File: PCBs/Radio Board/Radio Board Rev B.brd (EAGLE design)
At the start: 95.9 x 90.2 mm, 4 parts

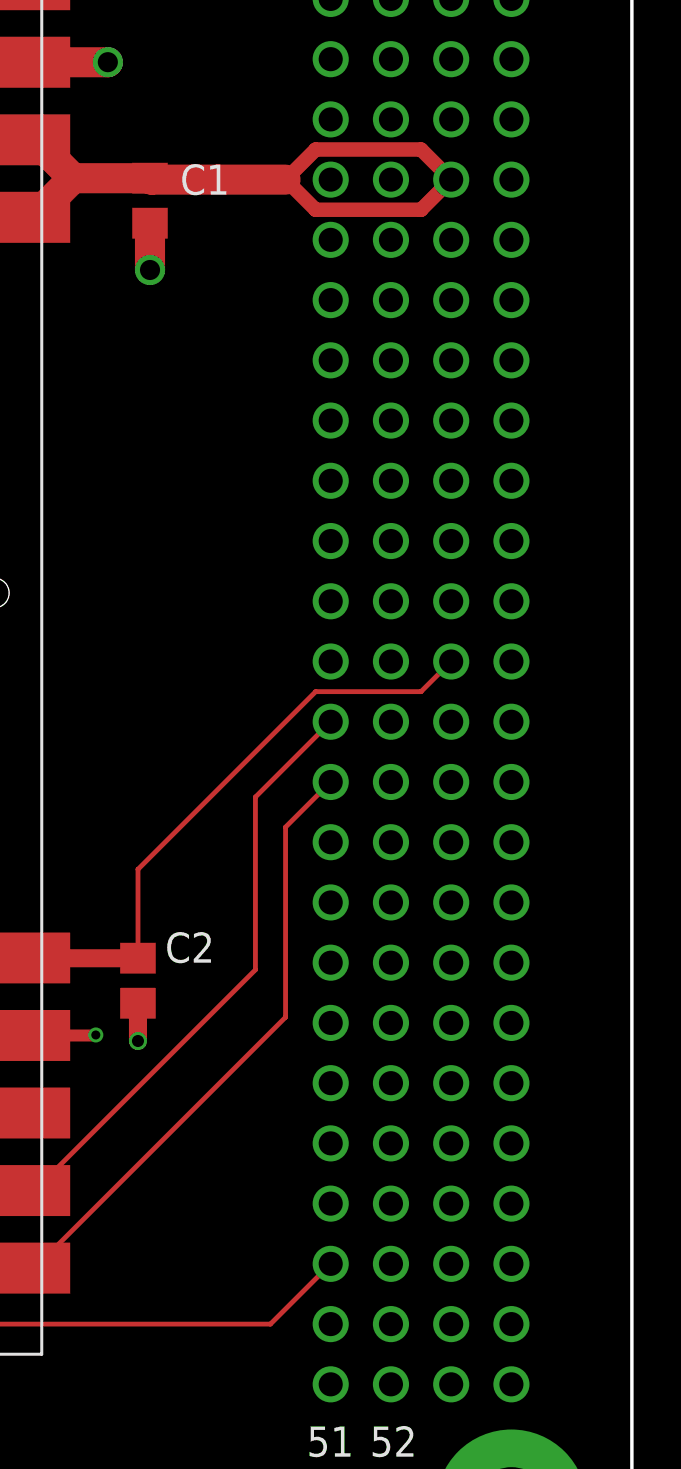
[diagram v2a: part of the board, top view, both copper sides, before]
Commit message: Use common PC104 footprint with dimensions set per board
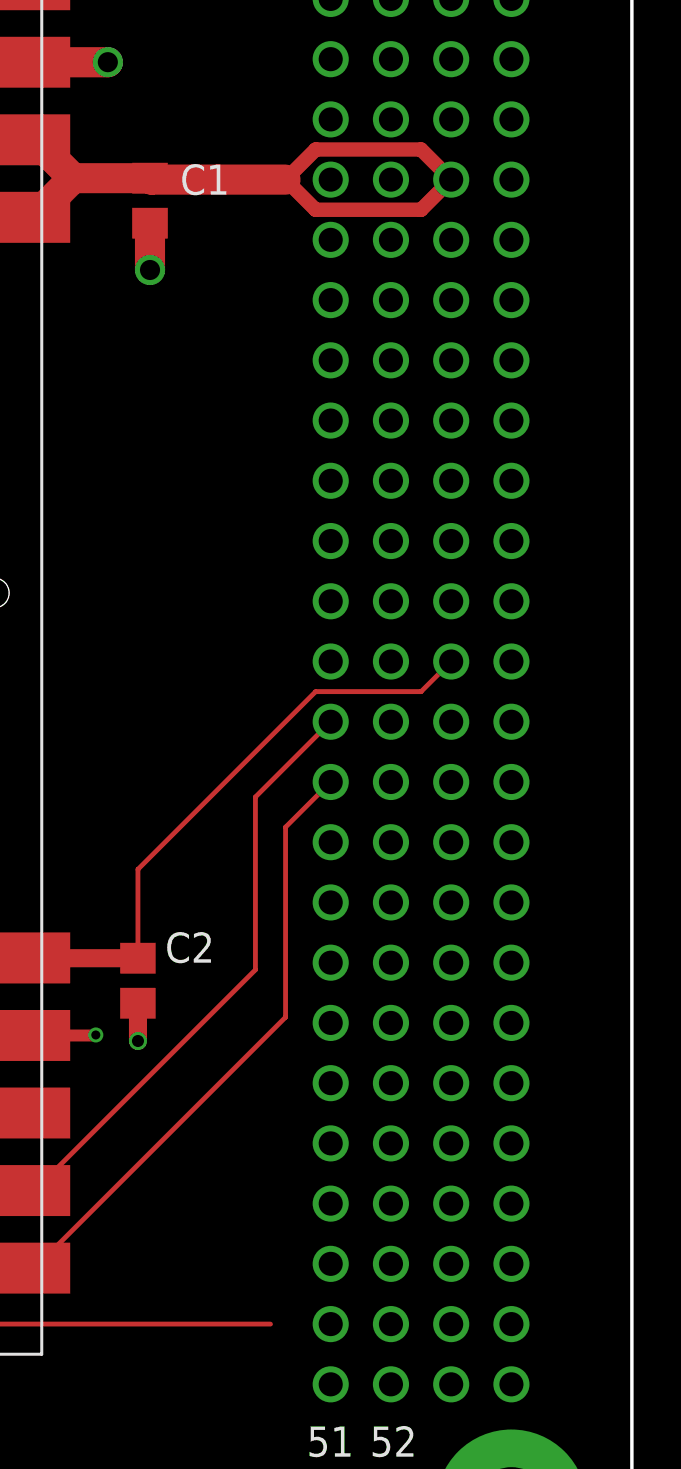
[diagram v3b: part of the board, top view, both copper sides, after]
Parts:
- removed U$2: PC104_RADIO, Cubesat:PC104_RADIO
- added U$1: PC104_NO_DIMENSION, Cubesat:PC104_NO_DIMENSION
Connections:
- net 3V3: now also U$1.79; no longer U$2.79
- net GND: now also U$1.100, U$1.61, U$1.66, U$1.69, U$1.73, U$1.74, U$1.81, U$1.82, U$1.84, U$1.99; no longer U$2.100, U$2.61, U$2.66, U$2.69, U$2.73, U$2.74, U$2.81, U$2.82, U$2.84, U$2.99
- net LITHIUM_RX: now also U$1.29; no longer U$2.29
- net LITHIUM_TX: now also U$1.31; no longer U$2.31
- net OA_RESET: now also U$1.47; no longer U$2.47
- net SW3: now also U$1.63; no longer U$2.63
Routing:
- net OA_RESET: track 46.8 -> 43.2 mm
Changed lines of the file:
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@@
 <board>
 <plain>
+<wire x1="0" y1="85.09" x2="0" y2="5.08" width="0.127" layer="20"/>
+<wire x1="0" y1="5.08" x2="5.08" y2="0" width="0.127" layer="20" curve="90"/>
+<wire x1="5.08" y1="0" x2="90.805" y2="0" width="0.127" layer="20"/>
+<wire x1="90.805" y1="0" x2="95.885" y2="5.08" width="0.127" layer="20" curve="90"/>
+<wire x1="95.885" y1="5.08" x2="95.885" y2="85.09" width="0.127" layer="20"/>
+<wire x1="95.885" y1="85.09" x2="90.678" y2="90.17" width="0.127" layer="20" curve="91.414625"/>
+<wire x1="0" y1="85.09" x2="10.16" y2="85.09" width="0.127" layer="20" curve="-180"/>
+<wire x1="10.16" y1="85.09" x2="15.24" y2="80.01" width="0.127" layer="20" curve="90"/>
+<wire x1="15.24" y1="80.01" x2="31.75" y2="80.01" width="0.127" layer="20"/>
+<wire x1="31.75" y1="80.01" x2="36.83" y2="85.09" width="0.127" layer="20" curve="90"/>
+<wire x1="36.83" y1="85.09" x2="41.91" y2="90.17" width="0.127" layer="20" curve="-90"/>
+<wire x1="41.91" y1="90.17" x2="90.678" y2="90.17" width="0.127" layer="20"/>
 </plain>
 <attributes>
@@
 </element>
 <element name="LI-1" library="Cubesat" package="LI-1" value="LI-1" x="38.1" y="13.97"/>
-<element name="U$2" library="Cubesat" package="PC104_RADIO" value="PC104_RADIO" x="0" y="0"/>
+<element name="U$1" library="Cubesat" package="PC104_NO_DIMENSION" value="PC104_NO_DIMENSION" x="0" y="0"/>
 </elements>
 <signals>
@@
 <wire x1="73.752" y1="71.72" x2="73.787" y2="71.755" width="1.27" layer="1"/>
 <via x="73.787" y="71.755" extent="1-16" drill="0.846665625"/>
-<contactref element="U$2" pad="61"/>
-<contactref element="U$2" pad="74"/>
-<contactref element="U$2" pad="73"/>
-<contactref element="U$2" pad="66"/>
-<contactref element="U$2" pad="69"/>
-<contactref element="U$2" pad="81"/>
-<contactref element="U$2" pad="99"/>
-<contactref element="U$2" pad="82"/>
-<contactref element="U$2" pad="84"/>
-<contactref element="U$2" pad="100"/>
 <contactref element="LI-1" pad="THERM1"/>
 <contactref element="LI-1" pad="THERM2"/>
 <contactref element="LI-1" pad="THERM3"/>
 <contactref element="LI-1" pad="THERM4"/>
+<contactref element="U$1" pad="61"/>
+<contactref element="U$1" pad="74"/>
+<contactref element="U$1" pad="73"/>
+<contactref element="U$1" pad="66"/>
+<contactref element="U$1" pad="69"/>
+<contactref element="U$1" pad="81"/>
+<contactref element="U$1" pad="99"/>
+<contactref element="U$1" pad="82"/>
+<contactref element="U$1" pad="84"/>
+<contactref element="U$1" pad="100"/>
 <wire x1="45.72" y1="52.07" x2="54.4" y2="60.07" width="0" layer="19" extent="1-1"/>
 </signal>
@@
 <wire x1="72.319" y1="63.561" x2="70.7" y2="61.942" width="1.27" layer="1"/>
 <wire x1="70.7" y1="61.942" x2="70.7" y2="61.91" width="1.27" layer="1"/>
-<wire x1="86.995" y1="64.77" x2="82.55" y2="64.77" width="0.6096" layer="1"/>
-<wire x1="86.995" y1="62.23" x2="82.55" y2="62.23" width="0.6096" layer="1"/>
-<contactref element="U$2" pad="63"/>
-<wire x1="88.265" y1="63.5" x2="86.995" y2="64.77" width="0.6096" layer="1"/>
-<wire x1="88.265" y1="63.5" x2="86.995" y2="62.23" width="0.6096" layer="1"/>
+<wire x1="82.55" y1="64.77" x2="86.995" y2="64.77" width="0.6096" layer="1"/>
+<wire x1="82.55" y1="62.23" x2="86.995" y2="62.23" width="0.6096" layer="1"/>
+<contactref element="U$1" pad="63"/>
+<wire x1="86.995" y1="64.77" x2="88.265" y2="63.5" width="0.6096" layer="1"/>
+<wire x1="86.995" y1="62.23" x2="88.265" y2="63.5" width="0.6096" layer="1"/>
 </signal>
 <signal name="LITHIUM_TX">
@@
 <wire x1="81.28" y1="28.18" x2="70.7" y2="17.6" width="0.2032" layer="1"/>
 <wire x1="81.28" y1="36.195" x2="81.28" y2="28.18" width="0.2032" layer="1"/>
-<contactref element="U$2" pad="31"/>
+<contactref element="U$1" pad="31"/>
 <wire x1="83.185" y1="38.1" x2="81.28" y2="36.195" width="0.2032" layer="1"/>
 </signal>
 <signal name="LITHIUM_RX">
 <contactref element="LI-1" pad="RX_UART"/>
-<wire x1="80.01" y1="37.465" x2="80.01" y2="30.18" width="0.2032" layer="1"/>
+<wire x1="80.01" y1="30.18" x2="80.01" y2="37.465" width="0.2032" layer="1"/>
 <wire x1="80.01" y1="30.18" x2="70.7" y2="20.87" width="0.2032" layer="1"/>
-<contactref element="U$2" pad="29"/>
-<wire x1="83.185" y1="40.64" x2="80.01" y2="37.465" width="0.2032" layer="1"/>
+<contactref element="U$1" pad="29"/>
+<wire x1="80.01" y1="37.465" x2="83.185" y2="40.64" width="0.2032" layer="1"/>
 </signal>
 <signal name="3V3">
@@
 <wire x1="82.55" y1="41.91" x2="75.057" y2="34.417" width="0.2032" layer="1"/>
 <wire x1="75.057" y1="34.417" x2="75.057" y2="30.668" width="0.2032" layer="1"/>
-<wire x1="86.995" y1="41.91" x2="82.55" y2="41.91" width="0.2032" layer="1"/>
-<contactref element="U$2" pad="79"/>
-<wire x1="88.265" y1="43.18" x2="86.995" y2="41.91" width="0.2032" layer="1"/>
+<wire x1="82.55" y1="41.91" x2="86.995" y2="41.91" width="0.2032" layer="1"/>
+<contactref element="U$1" pad="79"/>
+<wire x1="86.995" y1="41.91" x2="86.995" y2="41.91" width="0.2032" layer="1"/>
+<wire x1="86.995" y1="41.91" x2="88.265" y2="43.18" width="0.2032" layer="1"/>
 </signal>
 <signal name="OA_RESET">
@@
 <wire x1="38.4" y1="17.6" x2="40.76" y2="15.24" width="0.2032" layer="1"/>
 <wire x1="40.76" y1="15.24" x2="80.645" y2="15.24" width="0.2032" layer="1"/>
-<contactref element="U$2" pad="47"/>
-<wire x1="80.645" y1="15.24" x2="83.185" y2="17.78" width="0.2032" layer="1"/>
+<contactref element="U$1" pad="47"/>
+<wire x1="80.645" y1="15.24" x2="83.185" y2="17.78" width="0" layer="19" extent="1-1"/>
 </signal>
 </signals>

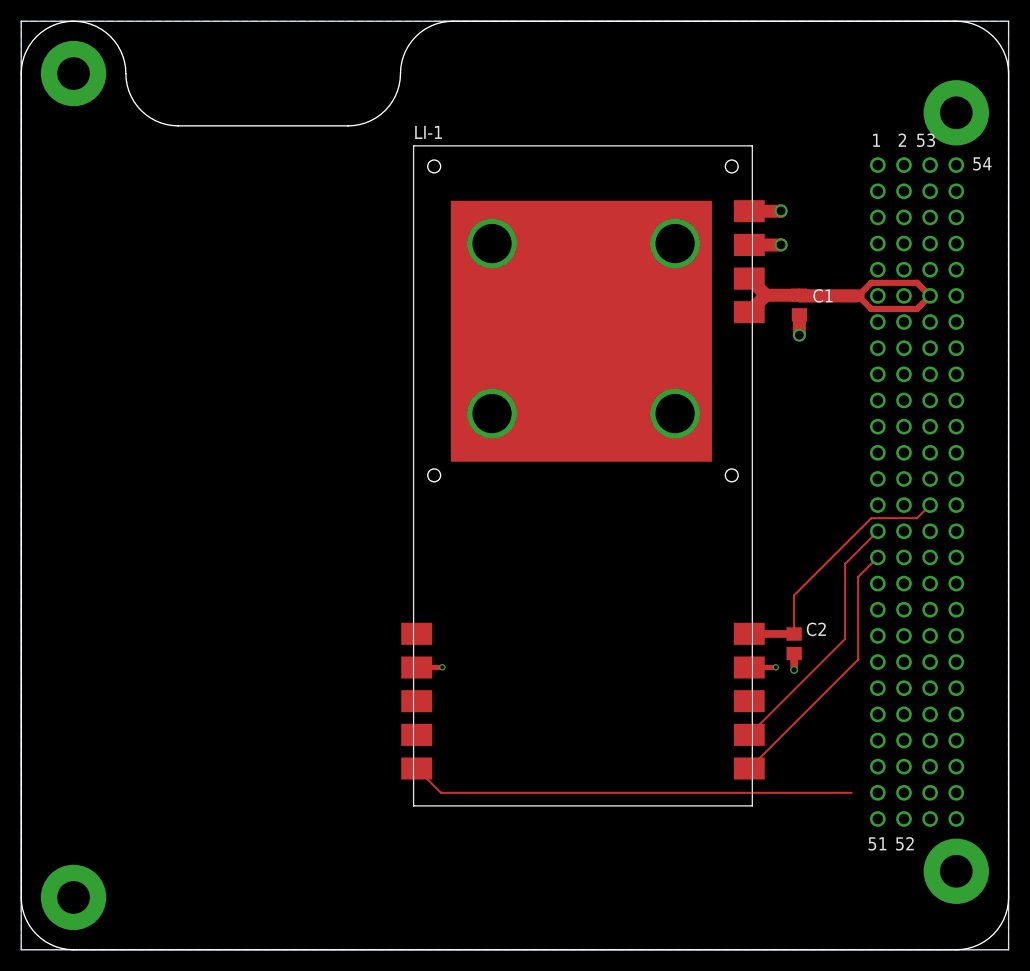
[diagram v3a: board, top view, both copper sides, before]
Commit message: Add test pads
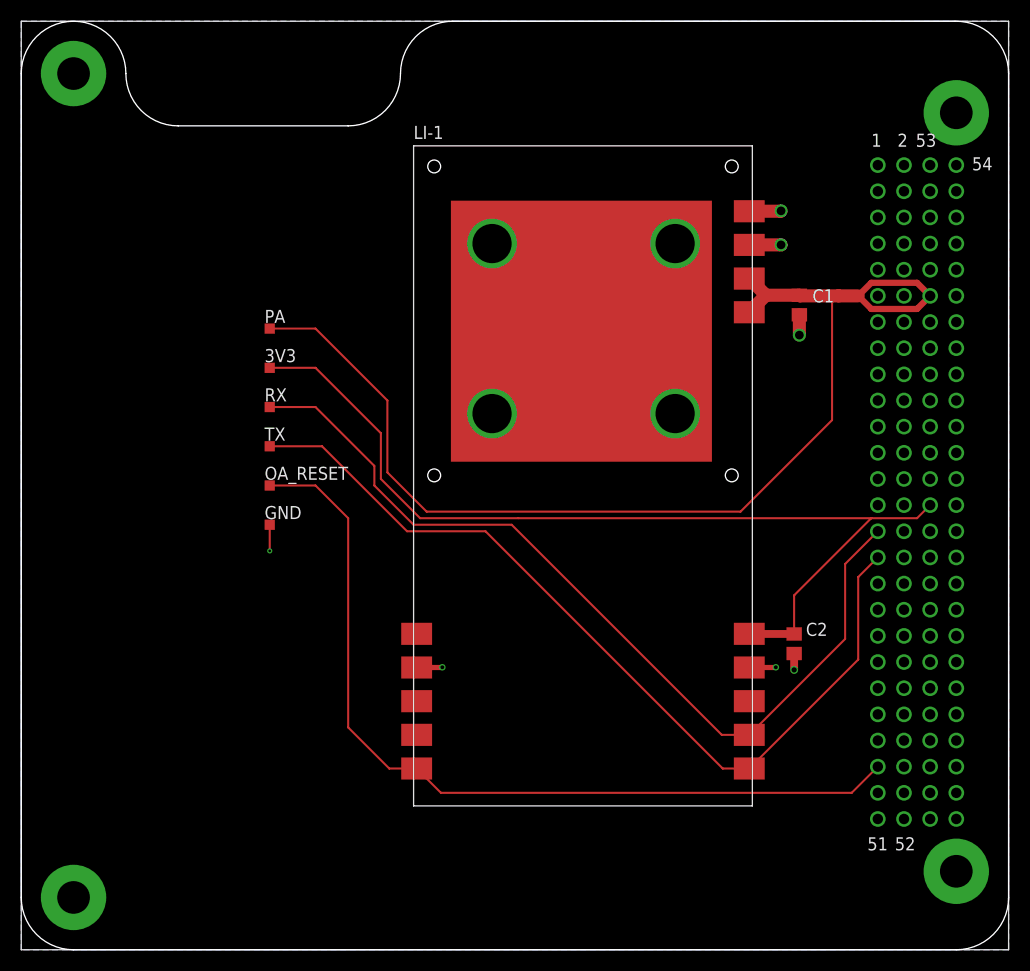
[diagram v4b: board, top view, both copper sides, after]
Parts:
- added 3V3, GND, OA_RESET, PA, RX, TX: TPTP10SQ, testpad:TP10SQ
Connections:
- removed net LITHIUM_RX: LI-1.RX_UART, U$1.29
- removed net LITHIUM_TX: LI-1.TX_UART, U$1.31
- new net LI_RX: LI-1.RX_UART, RX.TP, U$1.29
- new net LI_TX: LI-1.TX_UART, TX.TP, U$1.31
- net 3V3: now also 3V3.TP
- net GND: now also GND.TP
- net OA_RESET: now also OA_RESET.TP
- net SW3: now also PA.TP
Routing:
- net LI_RX: track 0.00 -> 85.8 mm
- net LI_TX: track 0.00 -> 85.2 mm
- net SW3: track 29.7 -> 111.7 mm
- net 3V3: track 24.9 -> 92.0 mm
- net OA_RESET: track 43.2 -> 84.4 mm
- net LITHIUM_TX: track 25.7 -> 0.00 mm
- net LITHIUM_RX: track 24.9 -> 0.00 mm
- net GND: track 14.8 -> 17.4 mm, vias 6 -> 7
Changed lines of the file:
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@@
 <element name="LI-1" library="Cubesat" package="LI-1" value="LI-1" x="38.1" y="13.97"/>
 <element name="U$1" library="Cubesat" package="PC104_NO_DIMENSION" value="PC104_NO_DIMENSION" x="0" y="0"/>
+<element name="3V3" library="testpad" library_urn="urn:adsk.eagle:library:385" package="TP10SQ" package3d_urn="urn:adsk.eagle:package:27962/1" value="TPTP10SQ" x="24.13" y="56.515">
+<attribute name="TP_SIGNAL_NAME" value="" x="24.13" y="56.515" size="1.778" layer="27" display="off"/>
+</element>
+<element name="RX" library="testpad" library_urn="urn:adsk.eagle:library:385" package="TP10SQ" package3d_urn="urn:adsk.eagle:package:27962/1" value="TPTP10SQ" x="24.13" y="52.705">
+<attribute name="TP_SIGNAL_NAME" value="" x="24.13" y="52.705" size="1.778" layer="27" display="off"/>
+</element>
+<element name="TX" library="testpad" library_urn="urn:adsk.eagle:library:385" package="TP10SQ" package3d_urn="urn:adsk.eagle:package:27962/1" value="TPTP10SQ" x="24.13" y="48.895">
+<attribute name="TP_SIGNAL_NAME" value="" x="24.13" y="48.895" size="1.778" layer="27" display="off"/>
+</element>
+<element name="OA_RESET" library="testpad" library_urn="urn:adsk.eagle:library:385" package="TP10SQ" package3d_urn="urn:adsk.eagle:package:27962/1" value="TPTP10SQ" x="24.13" y="45.085">
+<attribute name="TP_SIGNAL_NAME" value="" x="24.13" y="45.085" size="1.778" layer="27" display="off"/>
+</element>
+<element name="PA" library="testpad" library_urn="urn:adsk.eagle:library:385" package="TP10SQ" package3d_urn="urn:adsk.eagle:package:27962/1" value="TPTP10SQ" x="24.13" y="60.325">
+<attribute name="TP_SIGNAL_NAME" value="" x="24.13" y="60.325" size="1.778" layer="27" display="off"/>
+</element>
+<element name="GND" library="testpad" library_urn="urn:adsk.eagle:library:385" package="TP10SQ" package3d_urn="urn:adsk.eagle:package:27962/1" value="TPTP10SQ" x="24.13" y="41.275">
+<attribute name="TP_SIGNAL_NAME" value="" x="24.13" y="41.275" size="1.778" layer="27" display="off"/>
+</element>
 </elements>
 <signals>
@@
 <contactref element="U$1" pad="84"/>
 <contactref element="U$1" pad="100"/>
+<contactref element="GND" pad="TP"/>
+<wire x1="24.13" y1="41.275" x2="24.13" y2="38.735" width="0.2032" layer="1"/>
+<via x="24.13" y="38.735" extent="1-16" drill="0.254"/>
 <wire x1="45.72" y1="52.07" x2="54.4" y2="60.07" width="0" layer="19" extent="1-1"/>
 </signal>
@@
 <contactref element="LI-1" pad="V_AMP1"/>
 <contactref element="LI-1" pad="V_AMP2"/>
-<wire x1="81.28" y1="63.5" x2="75.626" y2="63.5" width="1.27" layer="1"/>
+<wire x1="81.28" y1="63.5" x2="79.375" y2="63.5" width="1.27" layer="1"/>
+<wire x1="79.375" y1="63.5" x2="75.626" y2="63.5" width="1.27" layer="1"/>
 <wire x1="75.626" y1="63.5" x2="75.565" y2="63.561" width="1.27" layer="1"/>
 <wire x1="75.565" y1="63.561" x2="72.319" y2="63.561" width="1.27" layer="1"/>
@@
 <wire x1="86.995" y1="64.77" x2="88.265" y2="63.5" width="0.6096" layer="1"/>
 <wire x1="86.995" y1="62.23" x2="88.265" y2="63.5" width="0.6096" layer="1"/>
+<contactref element="PA" pad="TP"/>
+<wire x1="79.375" y1="63.5" x2="78.74" y2="62.865" width="0.2032" layer="1"/>
+<wire x1="78.74" y1="62.865" x2="78.74" y2="51.435" width="0.2032" layer="1"/>
+<wire x1="78.74" y1="51.435" x2="69.85" y2="42.545" width="0.2032" layer="1"/>
+<wire x1="69.85" y1="42.545" x2="39.37" y2="42.545" width="0.2032" layer="1"/>
+<wire x1="39.37" y1="42.545" x2="35.56" y2="46.355" width="0.2032" layer="1"/>
+<wire x1="35.56" y1="46.355" x2="35.56" y2="53.34" width="0.2032" layer="1"/>
+<wire x1="35.56" y1="53.34" x2="28.575" y2="60.325" width="0.2032" layer="1"/>
+<wire x1="28.575" y1="60.325" x2="24.13" y2="60.325" width="0.2032" layer="1"/>
 </signal>
-<signal name="LITHIUM_TX">
-<contactref element="LI-1" pad="TX_UART"/>
-<wire x1="81.28" y1="28.18" x2="70.7" y2="17.6" width="0.2032" layer="1"/>
-<wire x1="81.28" y1="36.195" x2="81.28" y2="28.18" width="0.2032" layer="1"/>
-<contactref element="U$1" pad="31"/>
-<wire x1="83.185" y1="38.1" x2="81.28" y2="36.195" width="0.2032" layer="1"/>
-</signal>
-<signal name="LITHIUM_RX">
+<signal name="LI_RX">
 <contactref element="LI-1" pad="RX_UART"/>
 <wire x1="80.01" y1="30.18" x2="80.01" y2="37.465" width="0.2032" layer="1"/>
@@
 <contactref element="U$1" pad="29"/>
 <wire x1="80.01" y1="37.465" x2="83.185" y2="40.64" width="0.2032" layer="1"/>
+<contactref element="RX" pad="TP"/>
+<wire x1="70.7" y1="20.87" x2="68.03" y2="20.87" width="0.2032" layer="1"/>
+<wire x1="34.29" y1="45.085" x2="34.29" y2="46.99" width="0.2032" layer="1"/>
+<wire x1="34.29" y1="46.99" x2="28.575" y2="52.705" width="0.2032" layer="1"/>
+<wire x1="28.575" y1="52.705" x2="24.13" y2="52.705" width="0.2032" layer="1"/>
+<wire x1="68.03" y1="20.87" x2="47.625" y2="41.275" width="0.2032" layer="1"/>
+<wire x1="47.625" y1="41.275" x2="38.1" y2="41.275" width="0.2032" layer="1"/>
+<wire x1="38.1" y1="41.275" x2="34.29" y2="45.085" width="0.2032" layer="1"/>
 </signal>
 <signal name="3V3">
@@
 <wire x1="82.55" y1="41.91" x2="86.995" y2="41.91" width="0.2032" layer="1"/>
 <contactref element="U$1" pad="79"/>
-<wire x1="86.995" y1="41.91" x2="86.995" y2="41.91" width="0.2032" layer="1"/>
 <wire x1="86.995" y1="41.91" x2="88.265" y2="43.18" width="0.2032" layer="1"/>
+<contactref element="3V3" pad="TP"/>
+<wire x1="34.925" y1="45.72" x2="34.925" y2="50.165" width="0.2032" layer="1"/>
+<wire x1="34.925" y1="50.165" x2="28.575" y2="56.515" width="0.2032" layer="1"/>
+<wire x1="28.575" y1="56.515" x2="24.13" y2="56.515" width="0.2032" layer="1"/>
+<wire x1="48.26" y1="41.91" x2="38.735" y2="41.91" width="0.2032" layer="1"/>
+<wire x1="38.735" y1="41.91" x2="34.925" y2="45.72" width="0.2032" layer="1"/>
+<wire x1="82.55" y1="41.91" x2="48.26" y2="41.91" width="0.2032" layer="1"/>
 </signal>
 <signal name="OA_RESET">
@@
 <wire x1="40.76" y1="15.24" x2="80.645" y2="15.24" width="0.2032" layer="1"/>
 <contactref element="U$1" pad="47"/>
-<wire x1="80.645" y1="15.24" x2="83.185" y2="17.78" width="0" layer="19" extent="1-1"/>
+<contactref element="OA_RESET" pad="TP"/>
+<wire x1="80.645" y1="15.24" x2="83.185" y2="17.78" width="0.2032" layer="1"/>
+<wire x1="38.4" y1="17.6" x2="35.74" y2="17.6" width="0.2032" layer="1"/>
+<wire x1="28.575" y1="45.085" x2="24.13" y2="45.085" width="0.2032" layer="1"/>
+<wire x1="35.74" y1="17.6" x2="31.75" y2="21.59" width="0.2032" layer="1"/>
+<wire x1="31.75" y1="21.59" x2="31.75" y2="41.91" width="0.2032" layer="1"/>
+<wire x1="31.75" y1="41.91" x2="28.575" y2="45.085" width="0.2032" layer="1"/>
+</signal>
+<signal name="LI_TX">
+<contactref element="U$1" pad="31"/>
+<contactref element="TX" pad="TP"/>
+<contactref element="LI-1" pad="TX_UART"/>
+<wire x1="81.28" y1="28.18" x2="70.7" y2="17.6" width="0.2032" layer="1"/>
+<wire x1="81.28" y1="36.195" x2="81.28" y2="28.18" width="0.2032" layer="1"/>
+<wire x1="83.185" y1="38.1" x2="81.28" y2="36.195" width="0.2032" layer="1"/>
+<wire x1="70.7" y1="17.6" x2="68.125" y2="17.6" width="0.2032" layer="1"/>
+<wire x1="29.21" y1="48.895" x2="24.13" y2="48.895" width="0.2032" layer="1"/>
+<wire x1="68.125" y1="17.6" x2="45.085" y2="40.64" width="0.2032" layer="1"/>
+<wire x1="45.085" y1="40.64" x2="37.465" y2="40.64" width="0.2032" layer="1"/>
+<wire x1="37.465" y1="40.64" x2="29.21" y2="48.895" width="0.2032" layer="1"/>
 </signal>
 </signals>
